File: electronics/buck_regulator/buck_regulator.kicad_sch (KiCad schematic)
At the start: 28 parts, among them J1 VIN, J2 VOUT+, J3 VOUT-, Q1 Q_PMOS_DGS, U1 LTC3824EMSEPBF

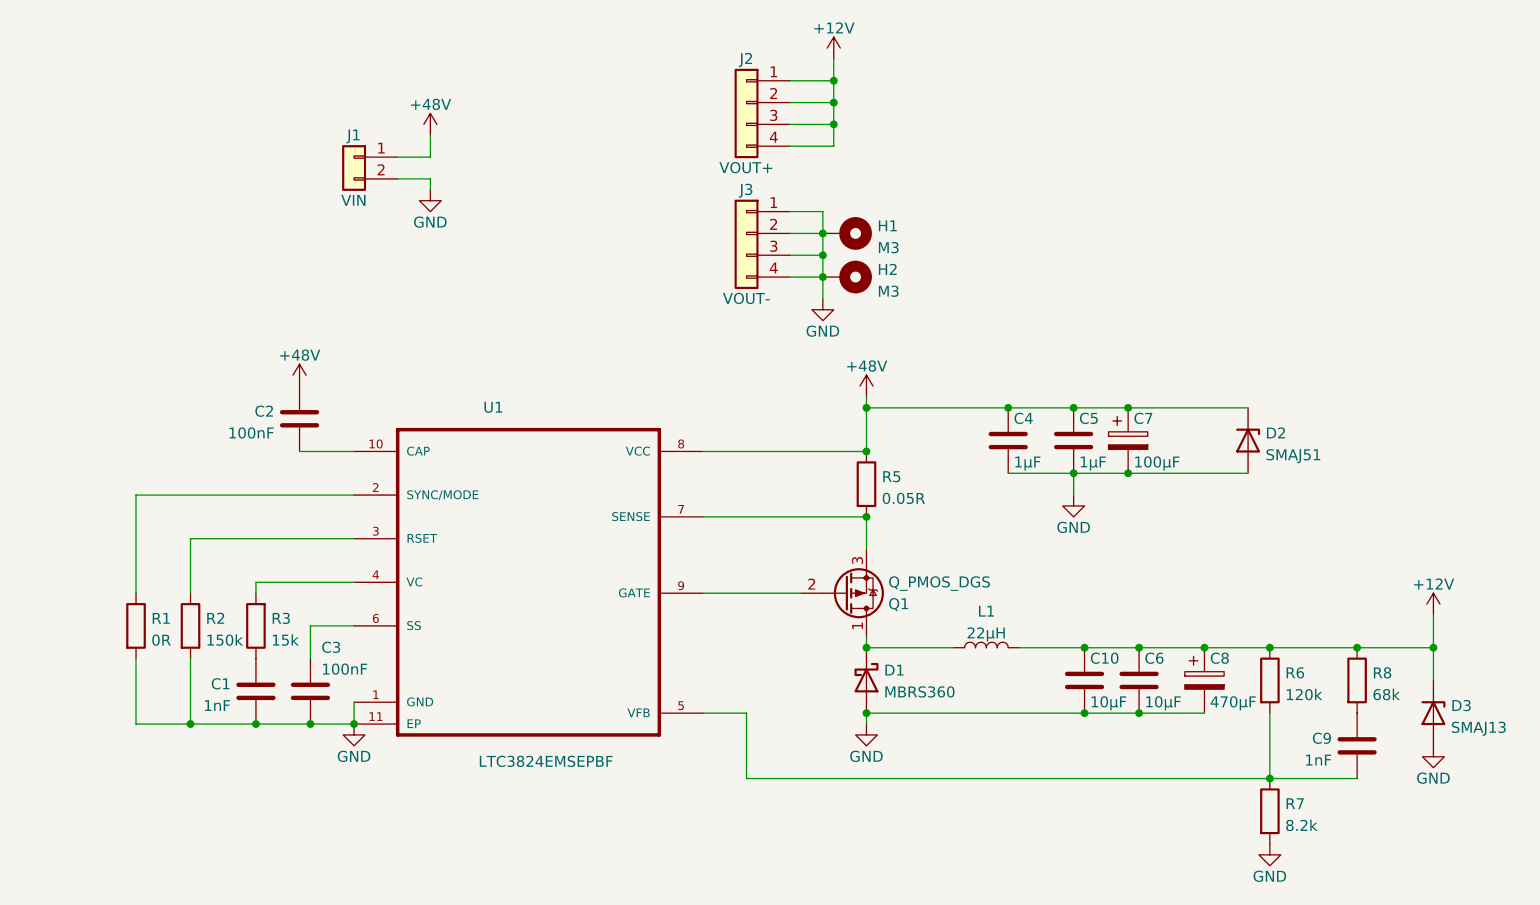
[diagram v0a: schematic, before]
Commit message: Buck regulator errata
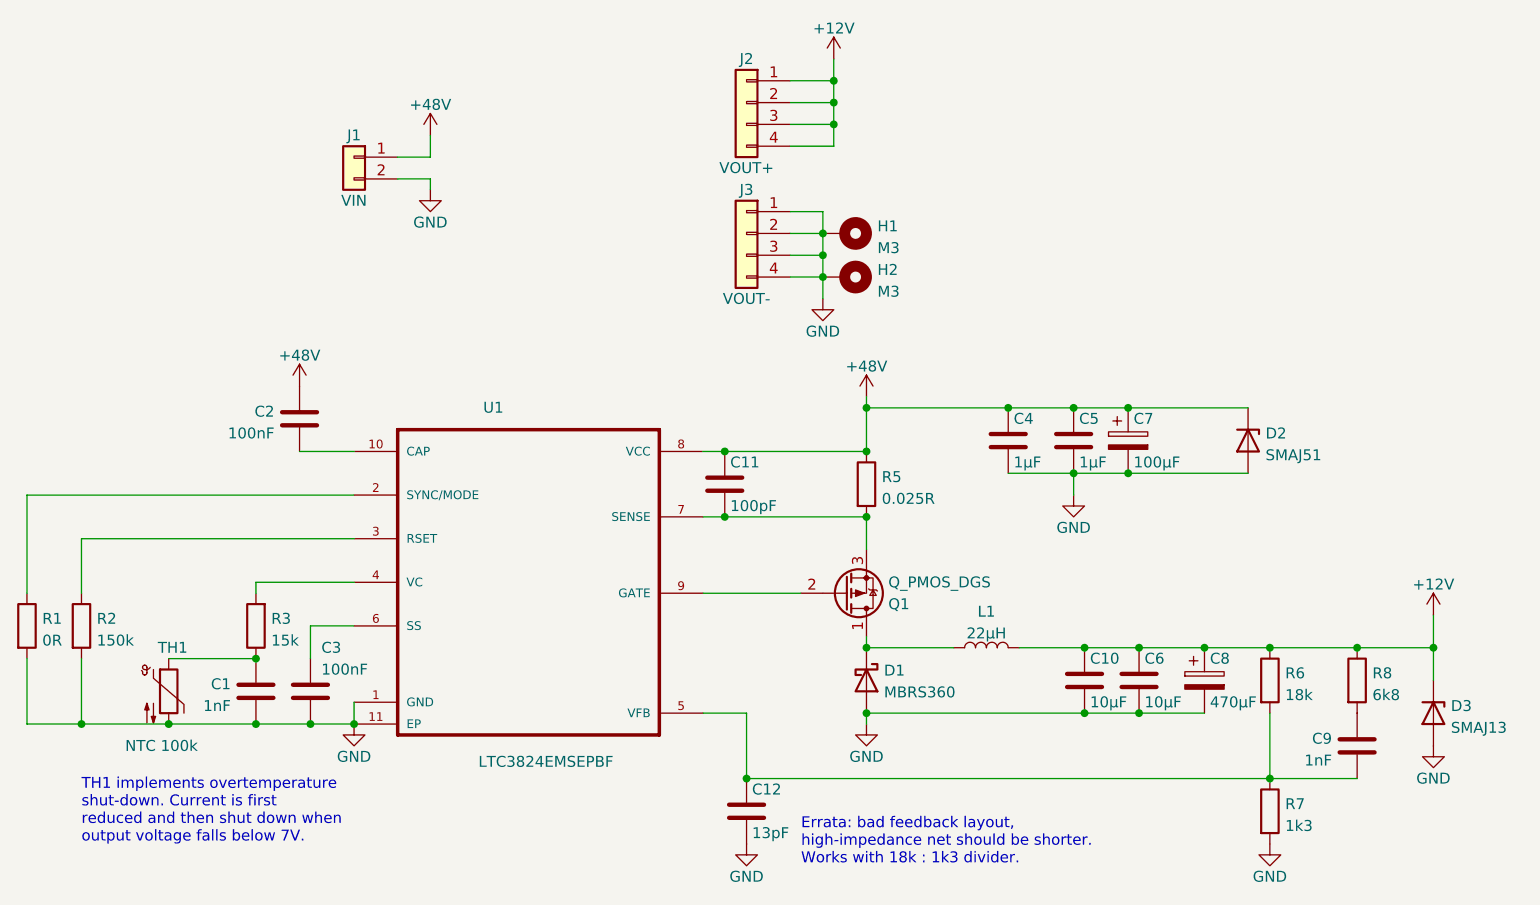
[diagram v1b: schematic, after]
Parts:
- added C11: 100pF, symbol Device:C
- added C12: 13pF, symbol Device:C
- added TH1: NTC 100k, symbol Device:Thermistor_NTC
- R5: value 0.05R -> 0.025R
- R6: value 120k -> 18k
- R7: value 8.2k -> 1k3
- R8: value 68k -> 6k8
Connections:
- net +48V: now also C11.1
- net GND: now also C12.2, TH1.2
- net at C1.1, R3.1: now also TH1.1
- net at Q1.3 (S), R5.2, U1.7 (SENSE): now also C11.2
- net at C9.2, R6.2, R7.1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: now also C12.1
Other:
- note added: "Errata: bad feedback layout, high-impedance net should be shorter. Works with 18k : 1k3 divider."
- note added: "TH1 implements overtemperature shut-down. Current is first reduced and then shut down when output voltage falls below 7V."
- moved on the sheet: R1, R2
